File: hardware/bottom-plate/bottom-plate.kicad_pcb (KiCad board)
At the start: 2 copper layers, 77.2 x 77.2 mm, 5 parts

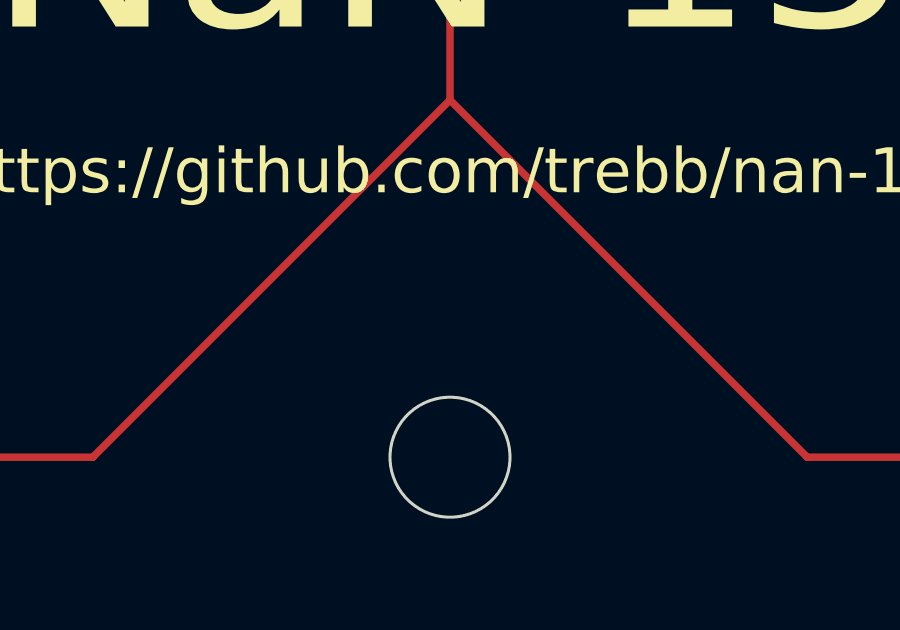
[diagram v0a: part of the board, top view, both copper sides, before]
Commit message: Connect all PWM pins to LEDs; show PCB version number
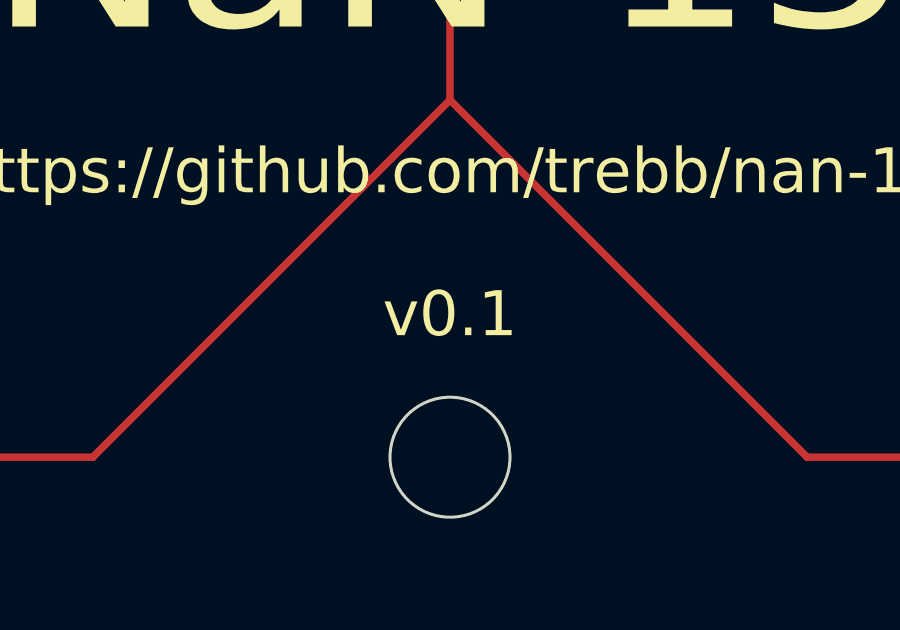
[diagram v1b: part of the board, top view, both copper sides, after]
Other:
- board text added: "v0.1"
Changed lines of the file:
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@@
     (area 107.15625 59.53125 192.881251 145.256251)
     (thickness 1.6)
-    (drawings 30)
+    (drawings 31)
     (tracks 29)
     (zones 0)
@@
       (xy 0.500964 3.601424)) (layer B.SilkS) (width 0.01))
   )
+  (gr_text v0.1 (at 150.01875 126.20625) (layer F.SilkS)
+    (effects (font (size 1.5 1.5) (thickness 0.3)))
+  )
   (gr_text https://github.com/trebb/nan-15 (at 150.01875 107.15625) (layer B.SilkS)
